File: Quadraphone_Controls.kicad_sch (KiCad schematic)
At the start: 16 parts, among them SW1 SYNCH_SWITCH, SW2 DPDT_Switch

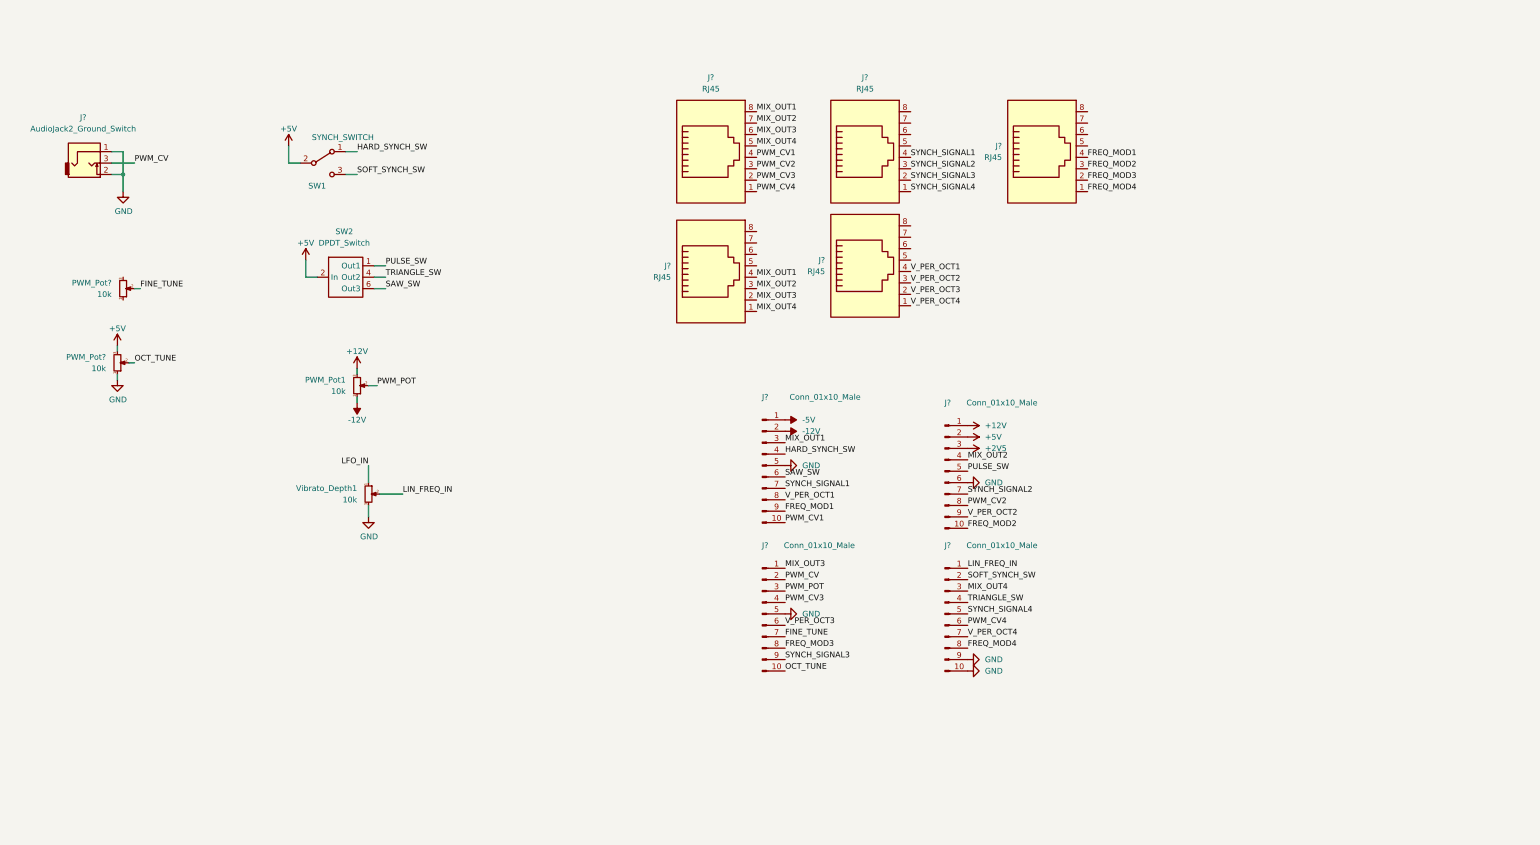
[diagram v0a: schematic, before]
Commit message: Started laying out control board
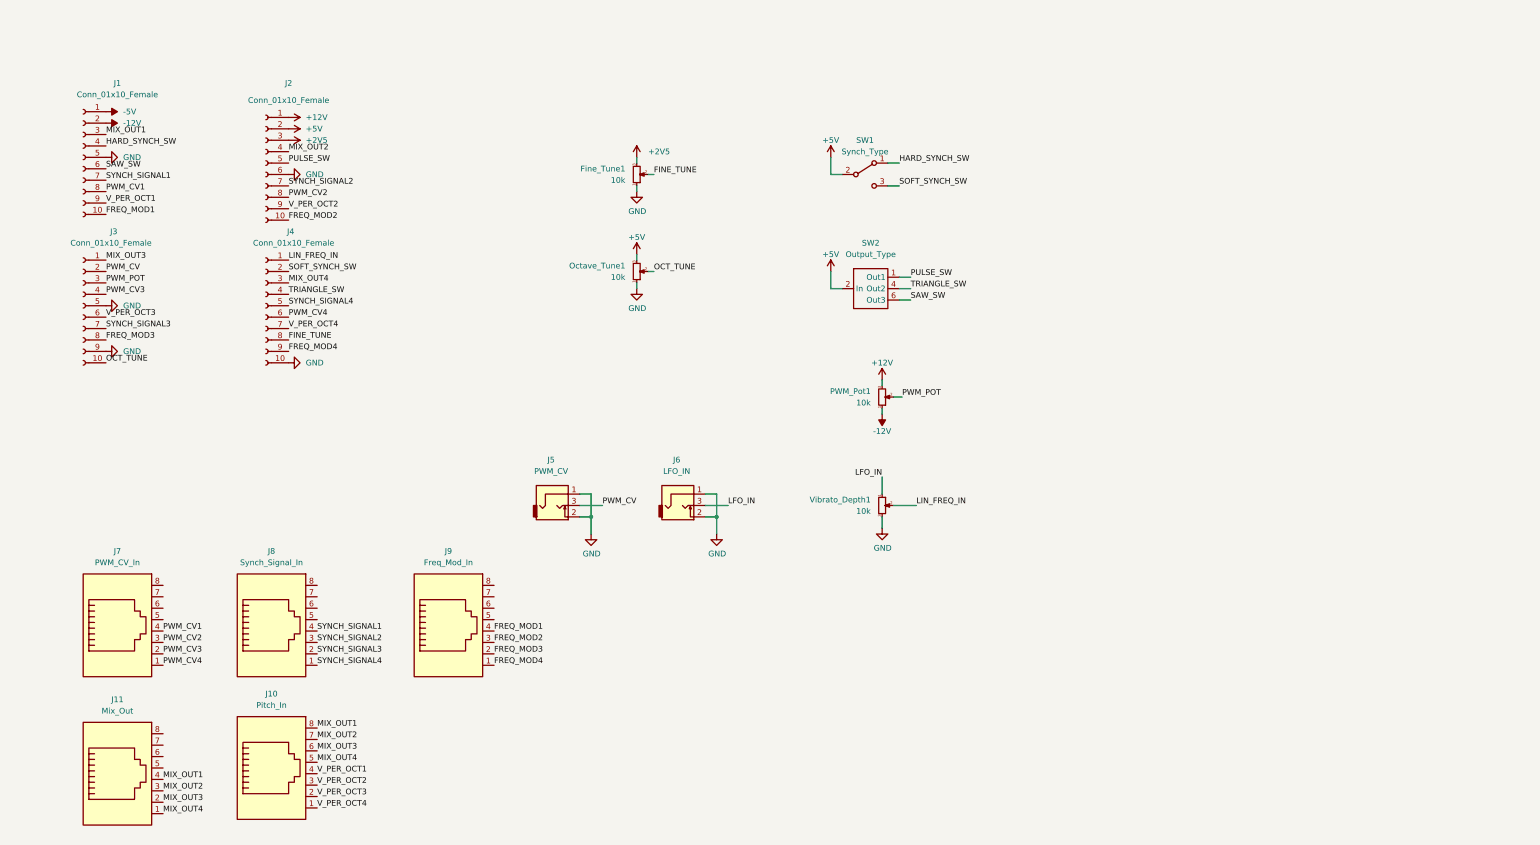
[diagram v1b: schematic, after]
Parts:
- removed J? (x4): Conn_01x10_Male, Connector_PinHeader_2.54mm:PinHeader_1x10_P2.54mm_Vertical, symbol Connector:Conn_01x10_Male
- added J1, J2, J3, J4: Conn_01x10_Female, Connector_PinSocket_2.54mm:PinSocket_1x10_P2.54mm_Vertical, symbol Connector:Conn_01x10_Female
- added J6: LFO_IN, Custom_Footprints:THONKICONN_hole, symbol thonkiconn:AudioJack2_Ground_Switch
- J10: renamed from J?; value RJ45 -> Pitch_In; footprint (none) -> Custom_Footprints:RJ45_Molex_42878-8506
- J11: renamed from J?; value RJ45 -> Mix_Out; footprint (none) -> Custom_Footprints:RJ45_Molex_42878-8506
- J5: renamed from J?; value AudioJack2_Ground_Switch -> PWM_CV; footprint (none) -> Custom_Footprints:THONKICONN_hole
- J7: renamed from J?; value RJ45 -> PWM_CV_In; footprint (none) -> Custom_Footprints:RJ45_Molex_42878-8506
- J8: renamed from J?; value RJ45 -> Synch_Signal_In; footprint (none) -> Custom_Footprints:RJ45_Molex_42878-8506
- J9: renamed from J?; value RJ45 -> Freq_Mod_In; footprint (none) -> Custom_Footprints:RJ45_Molex_42878-8506
- SW1: value SYNCH_SWITCH -> Synch_Type; footprint (none) -> Custom_Footprints:SPDTSubMiniature
- SW2: value DPDT_Switch -> Output_Type; footprint (none) -> Custom_Footprints:SW_100DP3T1B1M2QEH
- gave numbers to parts that had none: 2
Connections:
- net +12V: now also J2.1 (Pin_1)
- net +2V5: now also Fine_Tune1.3, J2.3 (Pin_3)
- net +5V: now also J2.2 (Pin_2)
- net -12V: now also J1.2 (Pin_2)
- net -5V: now also J1.1 (Pin_1)
- net FINE_TUNE: now also J4.8 (Pin_8)
- net FREQ_MOD1: now also J1.10 (Pin_10)
- net FREQ_MOD2: now also J2.10 (Pin_10)
- net FREQ_MOD3: now also J3.8 (Pin_8)
- net FREQ_MOD4: now also J4.9 (Pin_9)
- net GND: now also Fine_Tune1.1, J1.5 (Pin_5), J2.6 (Pin_6), J3.5 (Pin_5), J3.9 (Pin_9), J4.10 (Pin_10), J6.1, J6.2
- net HARD_SYNCH_SW: now also J1.4 (Pin_4)
- net LFO_IN: now also J6.3
- net LIN_FREQ_IN: now also J4.1 (Pin_1)
- net MIX_OUT1: now also J10.8, J1.3 (Pin_3); no longer J7.8
- net MIX_OUT2: now also J10.7, J2.4 (Pin_4); no longer J7.7
- net MIX_OUT3: now also J10.6, J3.1 (Pin_1); no longer J7.6
- net MIX_OUT4: now also J10.5, J4.3 (Pin_3); no longer J7.5
- net OCT_TUNE: now also J3.10 (Pin_10)
- net PULSE_SW: now also J2.5 (Pin_5)
- net PWM_CV: now also J3.2 (Pin_2)
- net PWM_CV1: now also J1.8 (Pin_8)
- net PWM_CV2: now also J2.8 (Pin_8)
- net PWM_CV3: now also J3.4 (Pin_4)
- net PWM_CV4: now also J4.6 (Pin_6)
- net PWM_POT: now also J3.3 (Pin_3)
- net SAW_SW: now also J1.6 (Pin_6)
- net SOFT_SYNCH_SW: now also J4.2 (Pin_2)
- net SYNCH_SIGNAL1: now also J1.7 (Pin_7)
- net SYNCH_SIGNAL2: now also J2.7 (Pin_7)
- net SYNCH_SIGNAL3: now also J3.7 (Pin_7)
- net SYNCH_SIGNAL4: now also J4.5 (Pin_5)
- net TRIANGLE_SW: now also J4.4 (Pin_4)
- net V_PER_OCT1: now also J1.9 (Pin_9)
- net V_PER_OCT2: now also J2.9 (Pin_9)
- net V_PER_OCT3: now also J3.6 (Pin_6)
- net V_PER_OCT4: now also J4.7 (Pin_7)
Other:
- moved on the sheet: Fine_Tune1, J10, J11, J5, J7, J8, J9, Octave_Tune1, PWM_Pot1, SW1, SW2, Vibrato_Depth1

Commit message: Started laying out Panel
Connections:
- net +2V5: no longer Fine_Tune1.3
- net +5V: now also Fine_Tune1.3
- net FINE_TUNE: now also J3.10 (Pin_10); no longer J4.8 (Pin_8)
- net OCT_TUNE: now also J4.8 (Pin_8); no longer J3.10 (Pin_10)
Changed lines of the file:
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@@
     (effects (font (size 1.27 1.27)) (justify left bottom))
   )
-  (label "OCT_TUNE" (at 34.29 91.44 0)
+  (label "OCT_TUNE" (at 74.93 86.36 0)
     (effects (font (size 1.27 1.27)) (justify left bottom))
   )
@@
     (effects (font (size 1.27 1.27)) (justify left bottom))
   )
-  (label "FINE_TUNE" (at 74.93 86.36 0)
+  (label "FINE_TUNE" (at 34.29 91.44 0)
     (effects (font (size 1.27 1.27)) (justify left bottom))
   )
@@
     (pin "8")
   )
+  (symbol (lib_id "power:+5V") (at 152.4 45.72 0) (unit 1)
+    (in_bom yes) (on_board yes)
+    (property "Reference" "#PWR0101" (id 0) (at 152.4 49.53 0)
+      (effects (font (size 1.27 1.27)) hide)
+    )
+    (property "Value" "+5V" (id 1) (at 152.4 41.91 0))
+    (property "Footprint" "" (id 2) (at 152.4 45.72 0)
+      (effects (font (size 1.27 1.27)) hide)
+    )
+    (property "Datasheet" "" (id 3) (at 152.4 45.72 0)
+      (effects (font (size 1.27 1.27)) hide)
+    )
+    (pin "1")
+  )
   (symbol (lib_id "power:GND") (at 74.93 91.44 90) (unit 1)
     (in_bom yes) (on_board yes) (fields_autoplaced)
@@
     (pin "3")
   )
-  (symbol (lib_id "power:+2V5") (at 152.4 45.72 0) (unit 1)
-    (in_bom yes) (on_board yes) (fields_autoplaced)
-    (property "Reference" "#PWR07" (id 0) (at 152.4 49.53 0)
-      (effects (font (size 1.27 1.27)) hide)
-    )
-    (property "Value" "+2V5" (id 1) (at 154.94 44.4499 0)
-      (effects (font (size 1.27 1.27)) (justify left))
-    )
-    (property "Footprint" "" (id 2) (at 152.4 45.72 0)
-      (effects (font (size 1.27 1.27)) hide)
-    )
-    (property "Datasheet" "" (id 3) (at 152.4 45.72 0)
-      (effects (font (size 1.27 1.27)) hide)
-    )
-    (pin "1")
-  )
   (symbol (lib_id "power:+5V") (at 195.58 45.72 0) (unit 1)
     (in_bom yes) (on_board yes)
@@
       (reference "#PWR06") (unit 1) (value "GND") (footprint "")
     )
-    (path "/f01cb584-8a0d-4eef-b1a6-375efa682fa6"
-      (reference "#PWR07") (unit 1) (value "+2V5") (footprint "")
-    )
     (path "/f3e69895-ceb2-4dc3-85de-7ad95c2eca6c"
       (reference "#PWR08") (unit 1) (value "+5V") (footprint "")
@@
       (reference "#PWR021") (unit 1) (value "GND") (footprint "")
     )
+    (path "/a6139c35-b8a0-4f5b-8dd4-c55f2c0d0f0b"
+      (reference "#PWR0101") (unit 1) (value "+5V") (footprint "")
+    )
     (path "/67772fca-577b-45de-bd17-feb9d04c0aaa"

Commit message: Refinements to panel and controls
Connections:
- net +5V: now also Fine_Tune1.1, Octave_Tune1.1; no longer Fine_Tune1.3, Octave_Tune1.3
- net GND: now also Fine_Tune1.3, Octave_Tune1.3; no longer Fine_Tune1.1, Octave_Tune1.1
- no-connect marks 0 -> 16
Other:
- moved on the sheet: Fine_Tune1, J1, J10, J11, J2, J3, J4, J5, J6, J7, J8, J9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

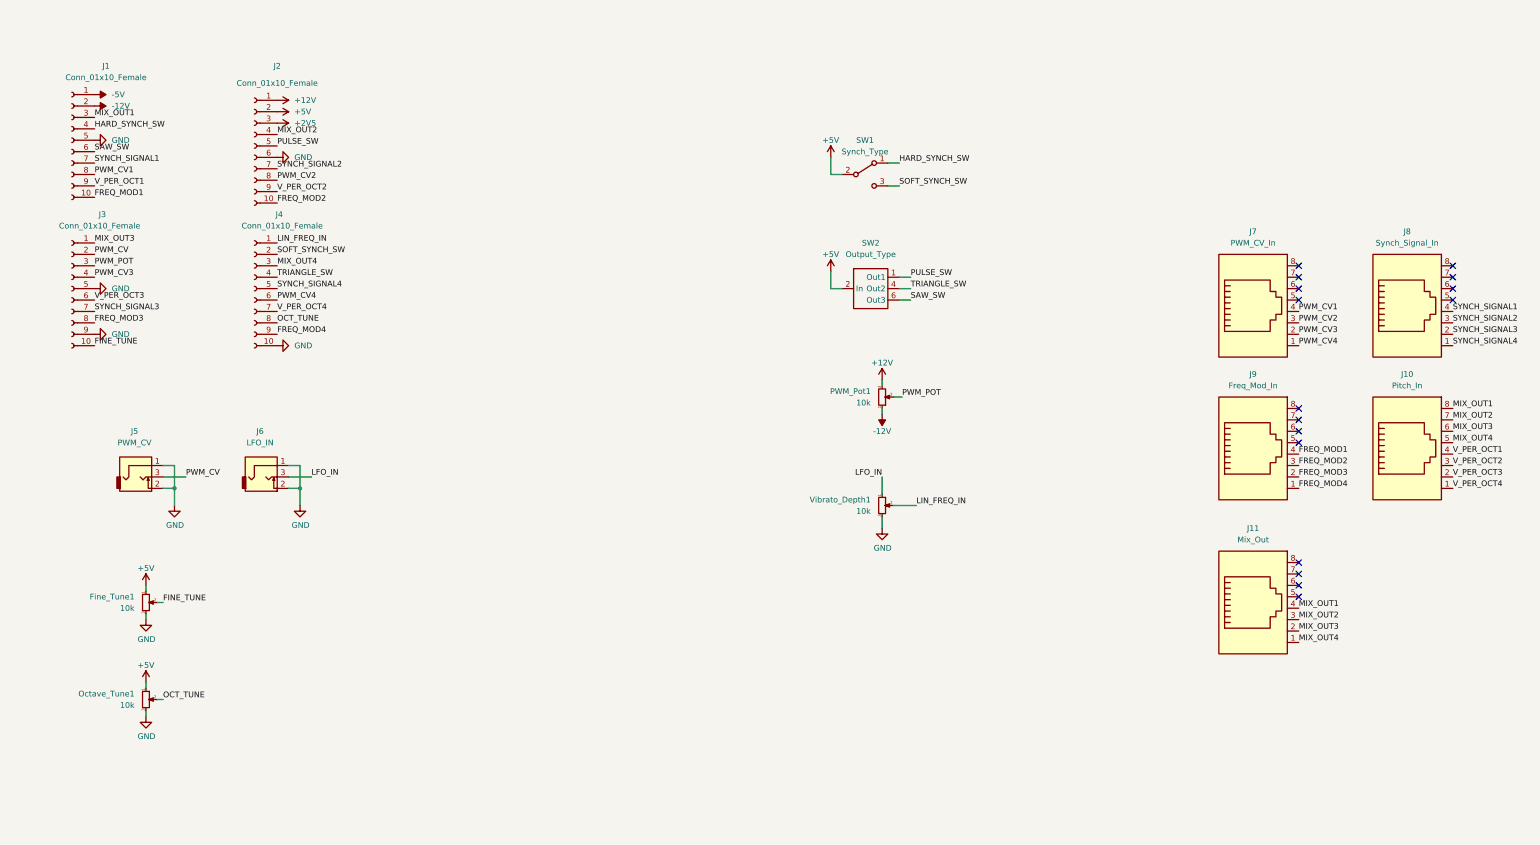
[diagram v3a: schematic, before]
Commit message: Fixed ground connections on component board
Added JLC PCB plug-in
Schematic clean-up
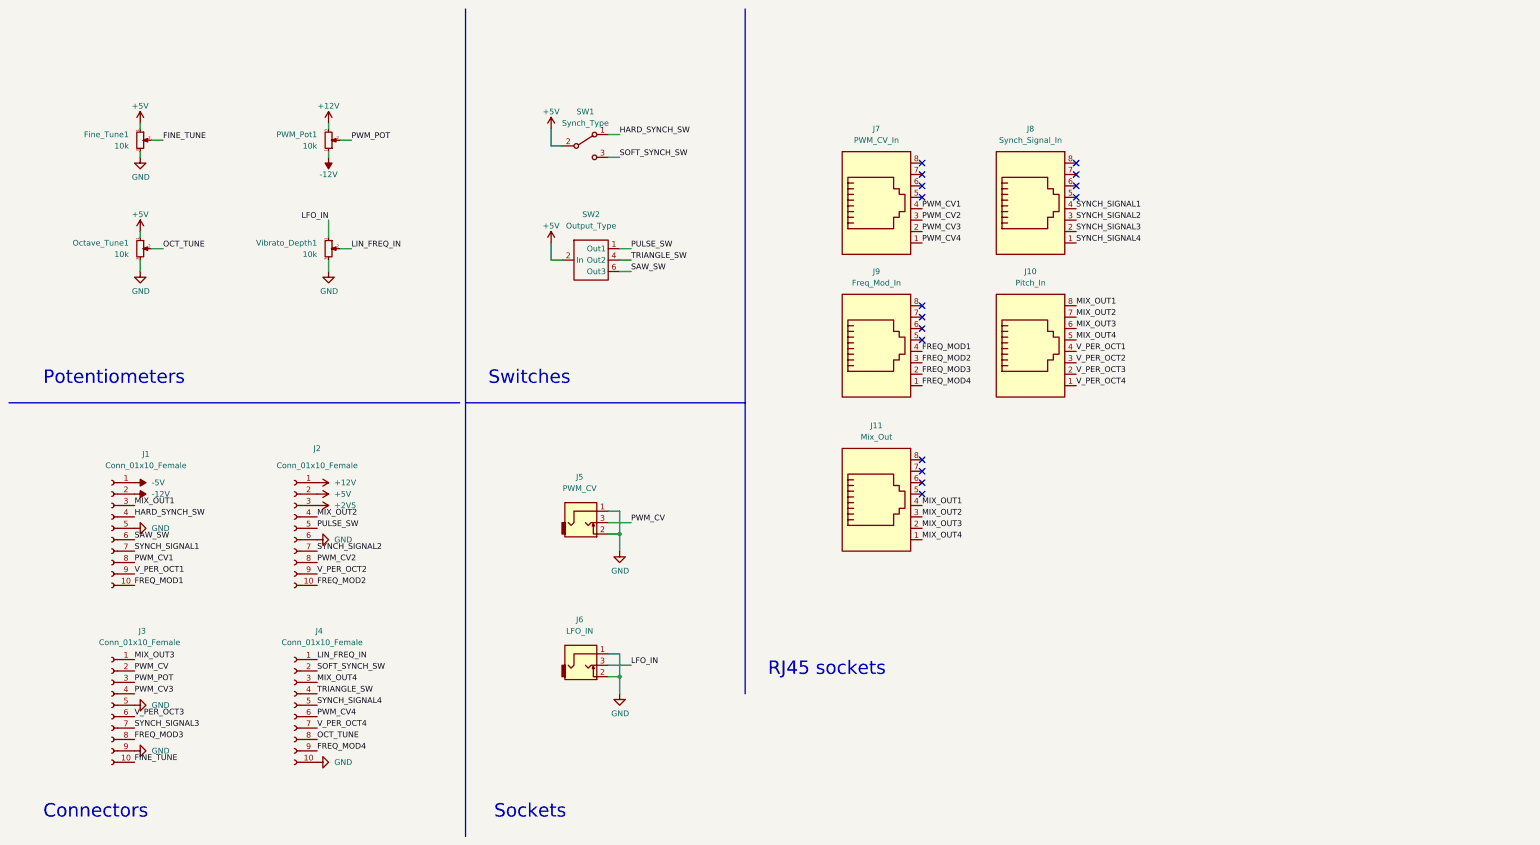
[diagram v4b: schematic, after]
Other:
- note added: "Connectors"
- note added: "Potentiometers"
- note added: "RJ45 sockets"
- note added: "Sockets"
- note added: "Switches"
- company: (none) -> Mountjoy Modular
- title: (none) -> Quadraphone Controls
- moved on the sheet: Fine_Tune1, J1, J10, J11, J2, J3, J4, J5, J6, J7, J8, J9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

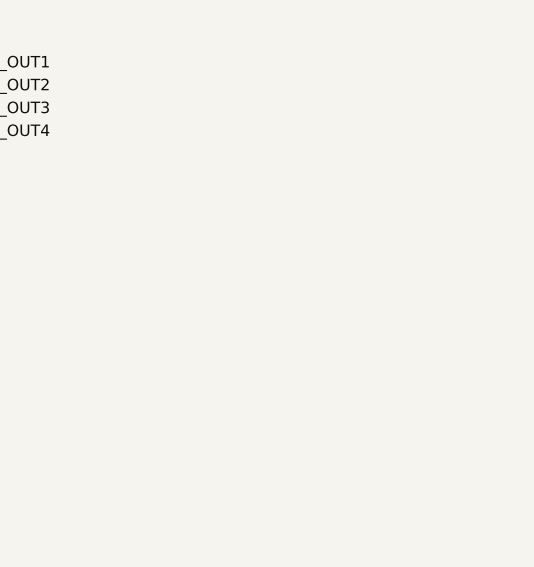
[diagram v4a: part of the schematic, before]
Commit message: Fixed issue with hole for voice switch size
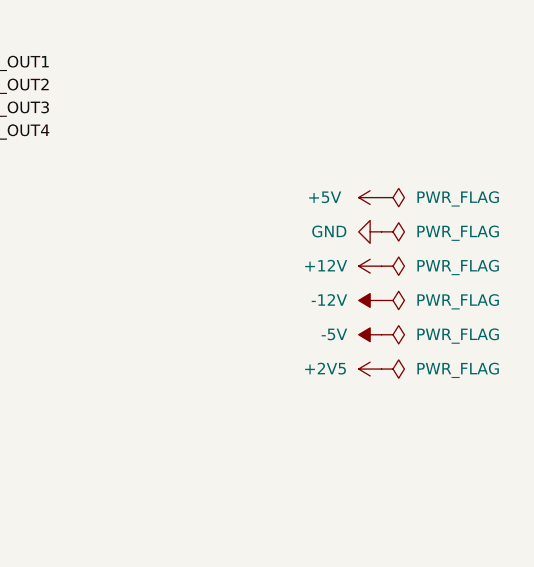
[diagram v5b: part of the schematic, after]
